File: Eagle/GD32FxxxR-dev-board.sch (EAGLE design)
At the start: 50 parts, among them J1 USART0, J2 VBat, J3 USB, J4 I2C1, J5 GPIOC, Q1 25MHz, Q2 32.768KHz, SW1 RESET, SW2 BOOT0, U1 GD32F207RX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

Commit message: Updated Add-on Pixel 8x 4 Universes
*. Added support for clock based led chip's (for example APA102)
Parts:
- removed J2: VBat, SparkFun-Connectors:CONN_02JST-PTH-2
- added J11: Vbat, SparkFun-Connectors:CONN_021X02_NO_SILK
- LED1: value LED1 -> PC0
- LED2: value LED2 -> PC2
- LED3: value LED3 -> PC3
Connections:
- net GND: now also J11.1; no longer J2.1
- net VBAT: now also J11.2; no longer J2.2
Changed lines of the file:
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@@
 <part name="GND4" library="supply1" library_urn="urn:adsk.eagle:library:371" deviceset="GND" device=""/>
 <part name="+3V2" library="supply1" library_urn="urn:adsk.eagle:library:371" deviceset="+3V3" device=""/>
-<part name="LED1" library="led" library_urn="urn:adsk.eagle:library:259" deviceset="LED" device="CHIP-LED0603" package3d_urn="urn:adsk.eagle:package:15819/3" value="LED1"/>
+<part name="LED1" library="led" library_urn="urn:adsk.eagle:library:259" deviceset="LED" device="CHIP-LED0603" package3d_urn="urn:adsk.eagle:package:15819/3" value="PC0"/>
 <part name="R2" library="rcl" library_urn="urn:adsk.eagle:library:334" deviceset="R-EU_" device="R0603" package3d_urn="urn:adsk.eagle:package:23555/3" value="10K">
 <spice>
@@
 <attribute name="JLCPCB" value="C44891"/>
 </part>
-<part name="LED2" library="led" library_urn="urn:adsk.eagle:library:259" deviceset="LED" device="CHIP-LED0603" package3d_urn="urn:adsk.eagle:package:15819/3" value="LED2"/>
-<part name="LED3" library="led" library_urn="urn:adsk.eagle:library:259" deviceset="LED" device="CHIP-LED0603" package3d_urn="urn:adsk.eagle:package:15819/3" value="LED3"/>
+<part name="LED2" library="led" library_urn="urn:adsk.eagle:library:259" deviceset="LED" device="CHIP-LED0603" package3d_urn="urn:adsk.eagle:package:15819/3" value="PC2"/>
+<part name="LED3" library="led" library_urn="urn:adsk.eagle:library:259" deviceset="LED" device="CHIP-LED0603" package3d_urn="urn:adsk.eagle:package:15819/3" value="PC3"/>
 <part name="LED4" library="led" library_urn="urn:adsk.eagle:library:259" deviceset="LED" device="CHIP-LED0603" package3d_urn="urn:adsk.eagle:package:15819/3" value="PWR"/>
 <part name="GND6" library="supply1" library_urn="urn:adsk.eagle:library:371" deviceset="GND" device=""/>
@@
 </part>
 <part name="GND22" library="supply1" library_urn="urn:adsk.eagle:library:371" deviceset="GND" device=""/>
-<part name="J2" library="SparkFun-Connectors" library_urn="urn:adsk.eagle:library:513" deviceset="CONN_02" device="JST-PTH-2" package3d_urn="urn:adsk.eagle:package:38053/1" value="VBat"/>
 <part name="GND23" library="supply1" library_urn="urn:adsk.eagle:library:371" deviceset="GND" device=""/>
 <part name="SV4" library="SparkFun-Connectors" library_urn="urn:adsk.eagle:library:513" deviceset="CONN_13" device="" package3d_urn="urn:adsk.eagle:package:38176/1" value="GPIO"/>
@@
 <part name="+3V11" library="supply1" library_urn="urn:adsk.eagle:library:371" deviceset="+3V3" device=""/>
 <part name="J5" library="SparkFun-Connectors" library_urn="urn:adsk.eagle:library:513" deviceset="CONN_03" device="" package3d_urn="urn:adsk.eagle:package:38063/1" value="GPIOC"/>
+<part name="J11" library="SparkFun-Connectors" library_urn="urn:adsk.eagle:library:513" deviceset="CONN_02" device="1X02_NO_SILK" package3d_urn="urn:adsk.eagle:package:38051/1" value="Vbat"/>
 </parts>
 <sheets>
@@
 <attribute name="VALUE" x="10.16" y="144.78" size="1.27" layer="96"/>
 </instance>
-<instance part="J2" gate="G$1" x="0" y="154.94" smashed="yes">
-<attribute name="VALUE" x="-2.54" y="150.114" size="1.778" layer="96" font="vector"/>
-<attribute name="NAME" x="-2.54" y="160.528" size="1.27" layer="95" font="vector"/>
-</instance>
 <instance part="GND23" gate="1" x="7.62" y="152.4" smashed="yes">
 <attribute name="VALUE" x="5.08" y="149.86" size="1.27" layer="96"/>
@@
 <attribute name="VALUE" x="27.94" y="94.234" size="1.778" layer="96" font="vector"/>
 <attribute name="NAME" x="27.94" y="107.188" size="1.778" layer="95" font="vector"/>
+</instance>
+<instance part="J11" gate="G$1" x="0" y="154.94" smashed="yes">
+<attribute name="VALUE" x="-2.54" y="150.114" size="1.778" layer="96" font="vector"/>
+<attribute name="NAME" x="-2.54" y="160.528" size="1.778" layer="95" font="vector"/>
 </instance>
 </instances>
@@
 <pinref part="C15" gate="G$1" pin="2"/>
 <pinref part="GND22" gate="1" pin="GND"/>
-</segment>
-<segment>
-<pinref part="GND23" gate="1" pin="GND"/>
-<pinref part="J2" gate="G$1" pin="1"/>
 </segment>
 <segment>
@@
 <wire x1="11.43" y1="96.52" x2="11.43" y2="95.25" width="0.1524" layer="91"/>
 </segment>
+<segment>
+<pinref part="GND23" gate="1" pin="GND"/>
+<pinref part="J11" gate="G$1" pin="1"/>
+</segment>
 </net>
 <net name="BOOT_RX" class="0">
@@
 <junction x="12.7" y="157.48"/>
 <label x="15.24" y="157.48" size="1.27" layer="95"/>
-<pinref part="J2" gate="G$1" pin="2"/>
 <wire x1="7.62" y1="157.48" x2="12.7" y2="157.48" width="0.1524" layer="91"/>
-</segment>
-</net>
+<pinref part="J11" gate="G$1" pin="2"/>
+</segment>
+</net>

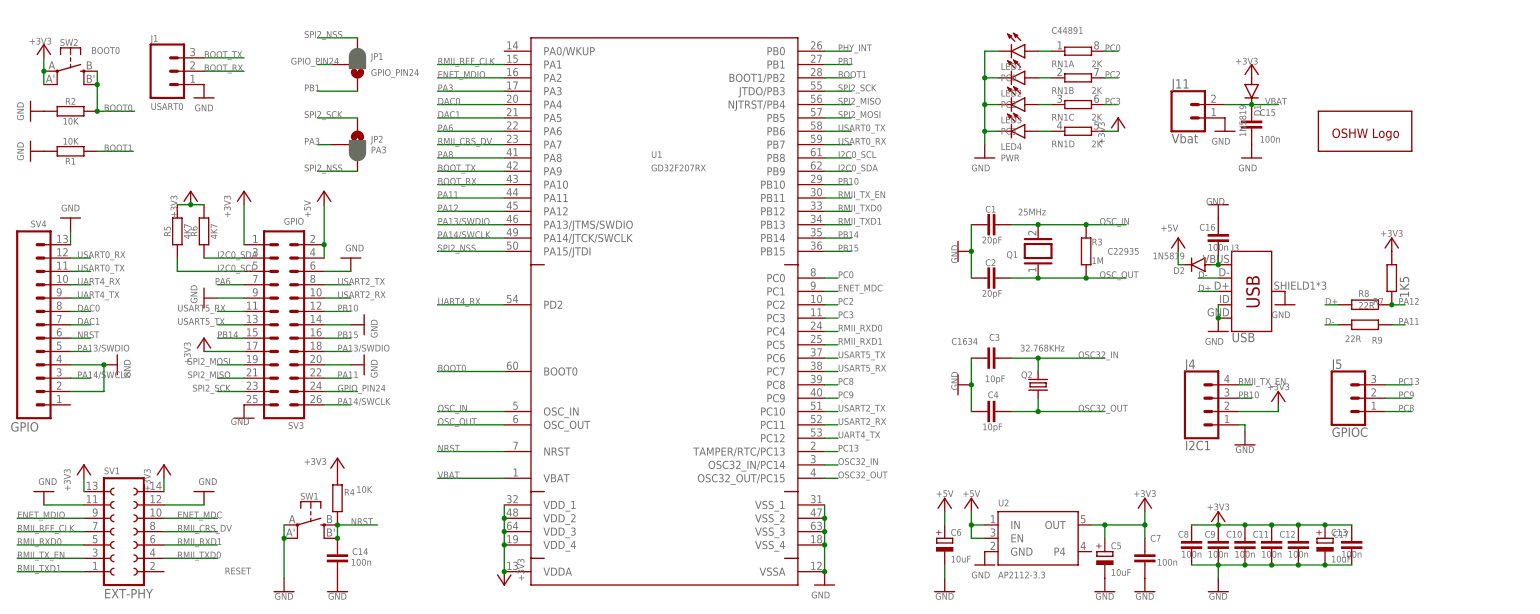
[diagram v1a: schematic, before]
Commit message: Added SPI Flash ROM
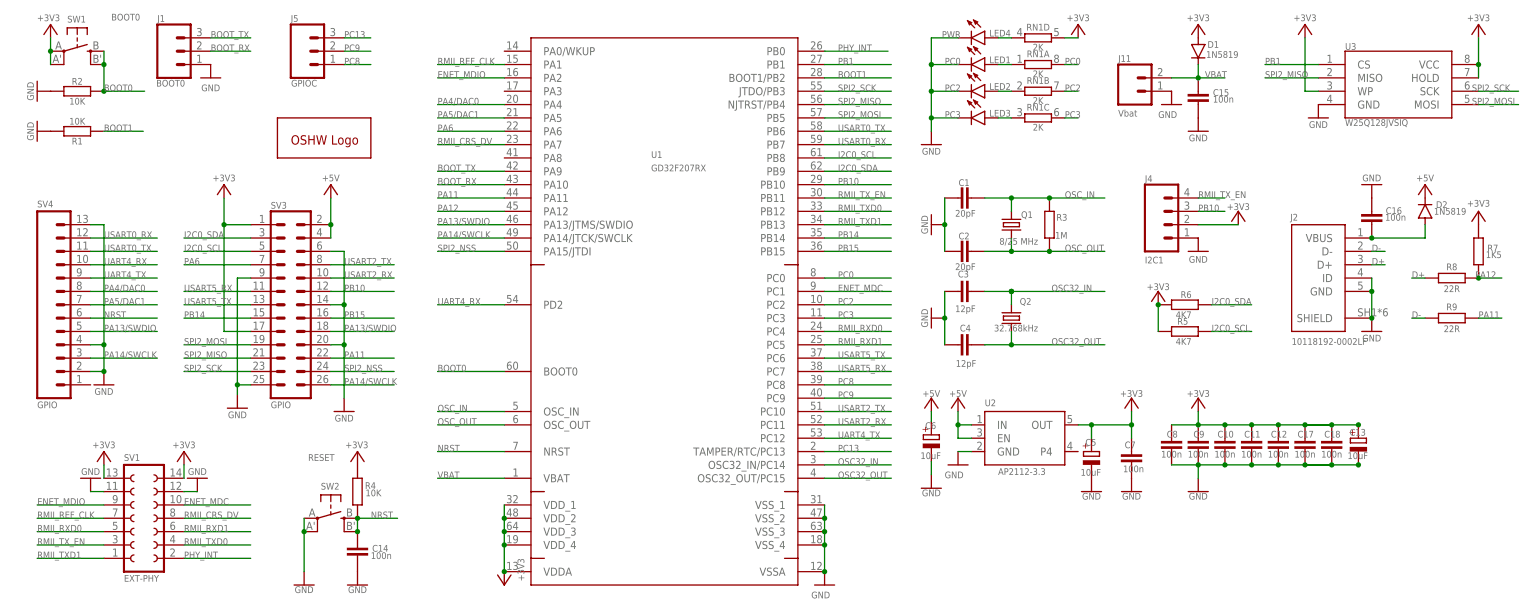
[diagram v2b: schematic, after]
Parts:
- removed J3: USB, USB-micro:USB_MICRO-B_FEMALE-SMT
- removed JP1: GPIO_PIN24, SparkFun-Jumpers:JUMPER-SMT_3_1-NC_PASTE_SILK
- removed JP2: PA3, SparkFun-Jumpers:JUMPER-SMT_3_1-NC_PASTE_SILK
- added C18: 100n, rcl:C-EUC0603
- added J2: 10118192-0002LF, USB connector:10118192-0002LF
- added U3: W25Q128JVSIQ, SparkFun-IC-Memory:SPI_FLASH-X25XXSMD1
- C1, C2: JLCPCB C1648 -> C38523
- C3, C4: value 10pF -> 12pF; JLCPCB C1634 -> C38523
- J1: value USART0 -> BOOT0
- Q1: value 25MHz -> 8/25 MHz; device special:XTAL/S -> crystal:CSM-7X-DU
- Q2: value 32.768KHz -> 32.768kHz; device crystal:CRYSTALTC26H -> crystal-geyer_V1_0:KX-327-NHT; JLCPCB (none) -> 32.768kHz
- SW1: value RESET -> BOOT0; JLCPCB (none) -> C221880
- SW2: value BOOT0 -> RESET; JLCPCB C221880 -> (none)
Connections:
- net DAC0 renamed PA4/DAC0
- net DAC1 renamed PA5/DAC1
- removed net GPIO_PIN24: JP1.2, SV3.24
- removed net PA3: JP2.2, U1.PA3
- removed net PA8: U1.PA8
- net +3V3: now also C18.1, SW1.P, SW1.P1, U3.HOLD, U3.VCC, U3.WP; no longer SW2.P, SW2.P1
- net BOOT0: now also SW1.S, SW1.S1; no longer SW2.S, SW2.S1
- net D+: now also J2.D+; no longer J3.D+
- net D-: now also J2.D-; no longer J3.D-
- net GND: now also C18.2, J2.GND, J2.ID, J2.SHIELD, SW2.P, SW2.P1, U3.GND; no longer J3.GND, J3.ID, J3.SHIELD, SW1.P, SW1.P1
- net NRST: now also SW2.S, SW2.S1; no longer SW1.S, SW1.S1
- net OSC_IN: now also R3.1; no longer R3.2
- net OSC_OUT: now also R3.2; no longer R3.1
- net PB1: now also U3.CS; no longer JP1.1
- net PHY_INT: now also SV1.2
- net SPI2_MISO: now also U3.MISO
- net SPI2_MOSI: now also U3.MOSI
- net SPI2_NSS: now also SV3.24; no longer JP1.3, JP2.3
- net SPI2_SCK: now also U3.SCK; no longer JP2.1
- net VBUS: now also J2.VBUS; no longer J3.VBUS
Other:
- moved on the sheet: C1, C10, C11, C12, C13, C14, C15, C16, C17, C2, C3, C4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
